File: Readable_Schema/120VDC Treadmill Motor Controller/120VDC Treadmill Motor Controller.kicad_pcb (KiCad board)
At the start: 2 copper layers, 171.2 x 90.5 mm, 60 parts, among them J1 TB005-762-03BE, J2 OSTT7020150, J3 TB0011-350-08BE, J4 TB0011-350-08BE, J5 TB0011-350-08BE, J6 TB0011-350-03BE, K1 T9GV1L14-24, Q1 IPP200N25N3GXKSA1, Q2 IPP200N25N3GXKSA1, Q3 IPP200N25N3GXKSA1, Q4 IPP200N25N3GXKSA1, U1 UCC21530DWKR, U2 UCC21530DWKR, U3 TMCS1126B42QDVGRQ1, U5 NLV14044BDR2G, U8 RAC05E-05SKT

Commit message: -Think we're finished with the schematic (finally) --Upped the LED resistors and added a few more supporting caps for the 3.3v iso supply in the feedback schema
-Started placing footprints
--Now that we're using how air instead of oven I'm not going to try and keep all SMD components on the same side anymore
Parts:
- removed R26: 10K, Resistor_SMD:R_0201_0603Metric_Pad0.64x0.40mm_HandSolder
- removed TP10, TP9: RCWCTE, Treadmill_Feet:RCWCTE
- removed U8: RAC05E-05SKT, Treadmill_Feet:RAC05E-KT_RCP
- added C14: 820uF, Treadmill_Feet:CHEMI-VSN_A45, F.Cu at (262.0, 117.4)
- added C17: 820uF, Treadmill_Feet:CHEMI-VSN_A45, F.Cu at (262.0, 154.0)
- added C18: 4.7u, Capacitor_SMD:C_0201_0603Metric_Pad0.64x0.40mm_HandSolder, F.Cu at (350.5, 57.8)
- added C19: 4.7u, Capacitor_SMD:C_0201_0603Metric_Pad0.64x0.40mm_HandSolder, F.Cu at (353.3, 43.8)
- added C20: 4.7u, Capacitor_SMD:C_0201_0603Metric_Pad0.64x0.40mm_HandSolder, F.Cu at (353.3, 45.6)
- added C21: 0.1u, Capacitor_SMD:C_0201_0603Metric_Pad0.64x0.40mm_HandSolder, F.Cu at (353.4, 113.8)
- added C22: 4.7u, Capacitor_SMD:C_0402_1005Metric_Pad0.74x0.62mm_HandSolder, F.Cu at (314.4, 54.1)
- added C23: 4.7u, Capacitor_SMD:C_0402_1005Metric_Pad0.74x0.62mm_HandSolder, F.Cu at (314.4, 56.1)
- added C24: 10u, Capacitor_SMD:C_0402_1005Metric_Pad0.74x0.62mm_HandSolder, F.Cu at (314.4, 58.1)
- added C25: 1u, Capacitor_SMD:C_0402_1005Metric_Pad0.74x0.62mm_HandSolder, F.Cu at (368.0, 61.9)
- added C26: 0.1u, Capacitor_SMD:C_0201_0603Metric_Pad0.64x0.40mm_HandSolder, F.Cu at (353.3, 47.3)
- added C27: 1u, Capacitor_SMD:C_0402_1005Metric_Pad0.74x0.62mm_HandSolder, F.Cu at (368.0, 63.9)
- added C28: C3216X7T2V104M160AA, Capacitor_SMD:C_1206_3216Metric_Pad1.33x1.80mm_HandSolder, F.Cu at (363.3, 44.6)
- added C29: 1uF, Capacitor_SMD:C_0201_0603Metric_Pad0.64x0.40mm_HandSolder, F.Cu at (353.4, 115.5)
- added C30: 22nF, Capacitor_SMD:C_0201_0603Metric_Pad0.64x0.40mm_HandSolder, F.Cu at (353.4, 117.3)
- added C31: 100pF, Capacitor_SMD:C_0201_0603Metric_Pad0.64x0.40mm_HandSolder, F.Cu at (353.4, 119.0)
- added C32: C3216X7T2V104M160AA, Capacitor_SMD:C_1206_3216Metric_Pad1.33x1.80mm_HandSolder, F.Cu at (363.3, 48.0)
- added C33: 100nF, Capacitor_SMD:C_0201_0603Metric_Pad0.64x0.40mm_HandSolder, F.Cu at (356.2, 112.0)
- added C34: 0.1u, Capacitor_SMD:C_0201_0603Metric_Pad0.64x0.40mm_HandSolder, F.Cu at (356.2, 113.8)
- added C35: 0.1u, Capacitor_SMD:C_0201_0603Metric_Pad0.64x0.40mm_HandSolder, F.Cu at (353.3, 49.1)
- added C36: 0.1u, Capacitor_SMD:C_0201_0603Metric_Pad0.64x0.40mm_HandSolder, F.Cu at (353.3, 50.8)
- added C37: 1u, Capacitor_SMD:C_0402_1005Metric_Pad0.74x0.62mm_HandSolder, F.Cu at (368.0, 65.8)
- added C38: 0.1u, Capacitor_SMD:C_0201_0603Metric_Pad0.64x0.40mm_HandSolder, F.Cu at (353.3, 52.6)
- added C39: 0.1u, Capacitor_SMD:C_0201_0603Metric_Pad0.64x0.40mm_HandSolder, F.Cu at (353.3, 54.3)
- added C40: 0.1u, Capacitor_SMD:C_0201_0603Metric_Pad0.64x0.40mm_HandSolder, F.Cu at (353.3, 56.1)
- added C41: 0.1u, Capacitor_SMD:C_0201_0603Metric_Pad0.64x0.40mm_HandSolder, F.Cu at (353.3, 57.8)
- added C42: 0.1u, Capacitor_SMD:C_0201_0603Metric_Pad0.64x0.40mm_HandSolder, F.Cu at (356.1, 43.8)
- added C43: 0.1u, Capacitor_SMD:C_0201_0603Metric_Pad0.64x0.40mm_HandSolder, F.Cu at (356.1, 45.6)
- added C44: 22n, Capacitor_SMD:C_0201_0603Metric_Pad0.64x0.40mm_HandSolder, B.Cu at (72.1, 87.0)
- added C45: 0.1u, Capacitor_SMD:C_0201_0603Metric_Pad0.64x0.40mm_HandSolder, F.Cu at (362.8, 92.5)
- added C46: 0.1u, Capacitor_SMD:C_0201_0603Metric_Pad0.64x0.40mm_HandSolder, F.Cu at (356.2, 115.5)
- added C47: 1uF, Capacitor_SMD:C_0201_0603Metric_Pad0.64x0.40mm_HandSolder, F.Cu at (356.2, 117.3)
- added C48: 100nF, Capacitor_SMD:C_0201_0603Metric_Pad0.64x0.40mm_HandSolder, F.Cu at (356.2, 119.0)
- added C49: C3216X7T2V104M160AA, Capacitor_SMD:C_1206_3216Metric_Pad1.33x1.80mm_HandSolder, F.Cu at (363.3, 51.3)
- added C50: C3216X7T2V104M160AA, Capacitor_SMD:C_1206_3216Metric_Pad1.33x1.80mm_HandSolder, F.Cu at (363.3, 54.7)
- added C51: C3216X7T2V104M160AA, Capacitor_SMD:C_1206_3216Metric_Pad1.33x1.80mm_HandSolder, F.Cu at (363.3, 58.0)
- added C52: C3216X7T2V104M160AA, Capacitor_SMD:C_1206_3216Metric_Pad1.33x1.80mm_HandSolder, F.Cu at (363.3, 61.4)
- added C53: C3216X7T2V104M160AA, Capacitor_SMD:C_1206_3216Metric_Pad1.33x1.80mm_HandSolder, F.Cu at (363.3, 64.7)
- added C54: C3216X7T2V104M160AA, Capacitor_SMD:C_1206_3216Metric_Pad1.33x1.80mm_HandSolder, F.Cu at (363.3, 68.1)
- added C6: 820uF, Treadmill_Feet:CHEMI-VSN_A45, F.Cu at (262.0, 44.4)
- added C7: 820uF, Treadmill_Feet:CHEMI-VSN_A45, F.Cu at (262.0, 80.9)
- added CR1: MMSZ5231B-7-F, Treadmill_Feet:SOD123_DIO, F.Cu at (354.8, 62.0)
- added CR2: MMSZ5231B-7-F, Treadmill_Feet:SOD123_DIO, F.Cu at (354.8, 65.0)
- added D3: MSS1P4-M3_89A, Treadmill_Feet:DIODE_MSS1P4-M3_89A, F.Cu at (369.1, 59.4)
- added D4: LED, LED_SMD:LED_1206_3216Metric_Pad1.42x1.75mm_HandSolder, F.Cu at (363.2, 73.5)
- added D5: SS12, Diode_SMD:D_SMA, B.Cu at (110.0, 65.0)
- added J7: OSTT7020150, Treadmill_Feet:CONN2_OSTT7020150_OST, F.Cu at (287.8, 55.2)
- added J9: OSTT7020150, Treadmill_Feet:CONN2_OSTT7020150_OST, F.Cu at (343.8, 90.4)
- added PS2: SRS-0509-2, Footprints_TMC:SRS-0515 DIP-16_W7.62mm, F.Cu at (349.9, 23.1)
- added PS7: IRM-15-5, Treadmill_Feet:CONV_IRM-15-5, F.Cu at (308.6, 35.5)
- added Q5: IPP60R060P7XKSA1, Package_TO_SOT_THT:TO-220-3_Vertical, F.Cu at (301.4, 60.8)
- added Q7: DN2450N8-G, Treadmill_Feet:TO-243AA_MCH, F.Cu at (358.3, 95.0)
- added Q8: VOM1271T, Treadmill_Feet:SOP-4_VIS, F.Cu at (358.9, 88.4)
- added R11: 100K, Resistor_SMD:R_0201_0603Metric_Pad0.64x0.40mm_HandSolder, B.Cu at (137.1, 122.0)
- added R12: 50, Resistor_SMD:R_0201_0603Metric_Pad0.64x0.40mm_HandSolder, B.Cu at (140.5, 118.1)
- added R17: 10K, Resistor_SMD:R_0201_0603Metric_Pad0.64x0.40mm_HandSolder, F.Cu at (356.1, 57.8)
- added R18: 10K, Resistor_SMD:R_0201_0603Metric_Pad0.64x0.40mm_HandSolder, B.Cu at (130.0, 120.9)
- added R19: 4.7, Resistor_SMD:R_1206_3216Metric_Pad1.30x1.75mm_HandSolder, F.Cu at (372.9, 29.4)
- added R20: 10, Resistor_SMD:R_1206_3216Metric_Pad1.30x1.75mm_HandSolder, F.Cu at (372.9, 32.7)
- added R21: 10, Resistor_SMD:R_1206_3216Metric_Pad1.30x1.75mm_HandSolder, F.Cu at (372.9, 36.0)
- added R22: 10, Resistor_SMD:R_1206_3216Metric_Pad1.30x1.75mm_HandSolder, F.Cu at (372.9, 39.3)
- added R28: 10K, Resistor_SMD:R_0201_0603Metric_Pad0.64x0.40mm_HandSolder, F.Cu at (320.2, 54.2)
- added R29: 10K, Resistor_SMD:R_0201_0603Metric_Pad0.64x0.40mm_HandSolder, B.Cu at (140.5, 136.1)
- added R30: 10K, Resistor_SMD:R_0201_0603Metric_Pad0.64x0.40mm_HandSolder, B.Cu at (140.5, 140.1)
- added R31: 1.2K, Resistor_SMD:R_0201_0603Metric_Pad0.64x0.40mm_HandSolder, F.Cu at (358.9, 49.1)
- added R32: 10K, Resistor_SMD:R_0201_0603Metric_Pad0.64x0.40mm_HandSolder, F.Cu at (358.9, 50.8)
- added R33: 30K, Treadmill_Feet:YAG_RSF100_YAG, F.Cu at (339.2, 75.1)
- added R34: 10K, Resistor_SMD:R_1206_3216Metric_Pad1.30x1.75mm_HandSolder, F.Cu at (355.0, 102.9)
- added R35: 500K, Resistor_SMD:R_1206_3216Metric_Pad1.30x1.75mm_HandSolder, F.Cu at (355.0, 106.2)
- added R36: 50, Resistor_SMD:R_0201_0603Metric_Pad0.64x0.40mm_HandSolder, F.Cu at (359.0, 115.5)
- added R37: 50, Resistor_SMD:R_0201_0603Metric_Pad0.64x0.40mm_HandSolder, F.Cu at (359.0, 117.3)
- added R38: 500K, Resistor_SMD:R_1206_3216Metric_Pad1.30x1.75mm_HandSolder, F.Cu at (355.0, 109.5)
- added R39: 10K, Resistor_SMD:R_0201_0603Metric_Pad0.64x0.40mm_HandSolder, B.Cu at (72.1, 81.0)
- added R40: 10K, Resistor_SMD:R_0201_0603Metric_Pad0.64x0.40mm_HandSolder, B.Cu at (72.1, 83.5)
- added R41: 3.3K, Resistor_SMD:R_0201_0603Metric_Pad0.64x0.40mm_HandSolder, B.Cu at (72.1, 132.5)
- added R42: 3.3K, Resistor_SMD:R_0201_0603Metric_Pad0.64x0.40mm_HandSolder, B.Cu at (72.1, 136.0)
- added R43: ERZ-V14D241, Treadmill_Feet:RES_ERZ-V14D241_PAN, F.Cu at (348.2, 130.8)
- added R45: 30K, Treadmill_Feet:YAG_RSF100_YAG, F.Cu at (339.2, 81.8)
- added R46: 330, Resistor_SMD:R_0201_0603Metric_Pad0.64x0.40mm_HandSolder, F.Cu at (362.8, 94.3)
- added R47: 1M, Resistor_SMD:R_0201_0603Metric_Pad0.64x0.40mm_HandSolder, F.Cu at (362.8, 96.0)
- added R48: 1K, Resistor_SMD:R_0201_0603Metric_Pad0.64x0.40mm_HandSolder, F.Cu at (362.8, 97.8)
- added R49: ERZ-V14D241, Treadmill_Feet:RES_ERZ-V14D241_PAN, F.Cu at (348.2, 137.5)
- added R50: ERZ-V14D241, Treadmill_Feet:RES_ERZ-V14D241_PAN, F.Cu at (348.2, 144.2)
- added R9: 10K, Resistor_SMD:R_0201_0603Metric_Pad0.64x0.40mm_HandSolder, F.Cu at (359.0, 112.0)
- added TP3: RCWCTE, Treadmill_Feet:RCWCTE, F.Cu at (354.9, 121.5)
- added U4: SN74HCS08DYYR, Treadmill_Feet:14-SOT-23-THIN, F.Cu at (360.8, 104.3)
- added U6: AMC1311BDWVR, Treadmill_Feet:DWV0008A, F.Cu at (344.4, 119.1)
- C1, C3, C9: value 33pF -> 33p
- C10, C16: value 0.1u -> 4.7u; footprint Capacitor_SMD:C_0402_1005Metric_Pad0.74x0.62mm_HandSolder -> Capacitor_SMD:C_0201_0603Metric_Pad0.64x0.40mm_HandSolder; moved to F.Cu
- C11: value 0.1u -> 33p; footprint Capacitor_SMD:C_0402_1005Metric_Pad0.74x0.62mm_HandSolder -> Capacitor_SMD:C_0201_0603Metric_Pad0.64x0.40mm_HandSolder
- C12: value 0.1u -> 33pF; footprint Capacitor_SMD:C_0402_1005Metric_Pad0.74x0.62mm_HandSolder -> Capacitor_SMD:C_0201_0603Metric_Pad0.64x0.40mm_HandSolder
- C13: value 33pF -> 0.1u
- C15: value 33pF -> 4.7u; moved to F.Cu
- C4: footprint Capacitor_SMD:C_0402_1005Metric_Pad0.74x0.62mm_HandSolder -> Capacitor_SMD:C_0201_0603Metric_Pad0.64x0.40mm_HandSolder; moved to F.Cu
- C5: footprint Capacitor_SMD:C_0402_1005Metric_Pad0.74x0.62mm_HandSolder -> Capacitor_SMD:C_0201_0603Metric_Pad0.64x0.40mm_HandSolder
- D2: value 1N5817 -> MSS1P4-M3_89A; footprint Diode_THT:D_DO-41_SOD81_P10.16mm_Horizontal -> Treadmill_Feet:DIODE_MSS1P4-M3_89A
- PS4: value SRS-0515-2 -> DHP1-5-S3-M; footprint Footprints_TMC:SRS-0515 DIP-16_W7.62mm -> Treadmill_Feet:CONV_DHP1-5-S3-M
- Q1, Q2, Q3, Q4: value IPP200N25N3GXKSA1 -> IPP60R060P7XKSA1
- R10: value 10K -> 4.7; footprint Resistor_SMD:R_0201_0603Metric_Pad0.64x0.40mm_HandSolder -> Resistor_SMD:R_1206_3216Metric_Pad1.30x1.75mm_HandSolder; moved to F.Cu
- R15: value 10K -> 10; footprint Resistor_SMD:R_0201_0603Metric_Pad0.64x0.40mm_HandSolder -> Resistor_SMD:R_1206_3216Metric_Pad1.30x1.75mm_HandSolder; moved to F.Cu
- R23, R27: moved to F.Cu
- R24: footprint Resistor_SMD:R_0201_0603Metric_Pad0.64x0.40mm_HandSolder -> Resistor_SMD:R_1206_3216Metric_Pad1.30x1.75mm_HandSolder; moved to F.Cu
- R25: value 10 -> 20K; moved to F.Cu
- R4: value 50 -> 10K
- R7: value 10 -> 1.2K; moved to F.Cu
- R8: value 10 -> 10K
- U5: value NLV14044BDR2G -> TPSI3050QDWZRQ1; footprint Treadmill_Feet:SOIC-16_ONS -> Treadmill_Feet:DWZ0008A-IPC_A; moved to F.Cu
- moved PS3 298.8 mm to (360.7, 23.1), turned to 0 degrees
- moved PS1 284.3 mm to (339.1, 23.1), turned to 0 degrees
- moved PS4 262.0 mm to (345.2, 108.4), turned to 0 degrees
- moved D2 260.9 mm to (369.1, 56.5), turned to 0 degrees
- moved C4 240.2 mm to (353.4, 112.0), turned to 0 degrees
- moved R15 230.0 mm to (372.9, 26.1)
- moved R23 222.9 mm to (359.0, 113.8), turned to 0 degrees
- moved C16 222.1 mm to (350.5, 56.1), turned to 0 degrees
- moved C15 217.3 mm to (350.5, 54.3), turned to 0 degrees
- moved R10 210.7 mm to (372.9, 22.7)
- moved U5 194.8 mm to (305.9, 53.3), turned to 0 degrees
- moved Q4 194.1 mm to (340.8, 64.7), turned to 0 degrees
- moved R25 188.9 mm to (320.2, 50.7)
- moved R7 187.8 mm to (356.1, 49.1)
- moved Q3 185.3 mm to (340.8, 58.8), turned to 0 degrees
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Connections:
- A1 pad 1: unconnected-(A1-GPIO0-Pad1) -> /Pi Pico/GP0
- A1 pad 11: unconnected-(A1-GPIO8-Pad11) -> Net-(A1-GPIO8)
- A1 pad 12: unconnected-(A1-GPIO9-Pad12)_1 -> Net-(A1-GPIO9)
- A1 pad 2: unconnected-(A1-GPIO1-Pad2) -> /Feedback/mcu_en
- A1 pad 26: unconnected-(A1-GPIO20-Pad26) -> /Pi Pico/pre_charge_mcu
- A1 pad 33: /Pi Pico/ADC_GND -> /Feedback/adc_gnd
- A1 pad 34: /Pi Pico/pot_adc -> /Feedback/cap_vsense
- C10 pad 1: /H_Bridge/hs_ps_2_+ -> /H_Bridge/ls_ps_+
- C10 pad 2: /H_Bridge/hs_ps_2_- -> /Feedback/in+
- C11 pad 1: /H_Bridge/hs_ps_1_+ -> Net-(U1-INB)
- C11 pad 2: /H_Bridge/hs_ps_1_- -> LV_GND
- C12 pad 1: /H_Bridge/ls_ps_+ -> Net-(U1-DT)
- C12 pad 2: HV_GND -> LV_GND
- C13 pad 1: Net-(U1-INB) -> 5v 15w
- C15 pad 1: Net-(U1-DT) -> /H_Bridge/hs_ps_2_+
- C15 pad 2: LV_GND -> Net-(J2-Pin_2)
- C16 pad 1: 5v 5w -> Net-(J2-Pin_2)
- C16 pad 2: LV_GND -> /H_Bridge/hs_ps_2_-
- C5 pad 1: 5v 5w -> 5v 15w
- D1 pad 1: 170V Rect -> Net-(D1-+)
- D2 pad 1: Net-(A1-VSYS) -> Net-(D2-Pad1)
- D2 pad 2: 5v 5w -> Net-(Q2-G)
- J1 pad 3: unconnected-(J1-Pin_3-Pad3) -> Net-(J1-Pin_3)
- J2 pad 1: /H_Bridge/hs_ps_1_- -> Net-(J2-Pin_1)
- J2 pad 2: /H_Bridge/hs_ps_2_- -> Net-(J2-Pin_2)
- J3 pad 1: 5v 5w -> 5v 15w
- J3 pad 5: 5v 5w -> 5v 15w
- J4 pad 1: /Pi Pico/pot_adc -> Net-(A1-GPIO8)
- J4 pad 2: /Pi Pico/ADC_GND -> Net-(A1-GPIO9)
- J5 pad 7: /Pi Pico/ADC_GND -> /Feedback/adc_gnd
- J5 pad 8: 3v3 MCU -> /Pi Pico/GP0
- J6 pad 3: 5v 5w -> 5v 15w
- JP2 pad 2: /Pi Pico/ADC_GND -> /Feedback/adc_gnd
- PS1 pad 1: 5v 5w -> 5v 15w
- PS1 pad 11: HV_GND -> /H_Bridge/hs_ps_1_-
- PS1 pad 7: /H_Bridge/ls_ps_+ -> /H_Bridge/hs_ps_1_+
- PS3 pad 1: 5v 5w -> 5v 15w
- PS3 pad 11: /H_Bridge/hs_ps_1_- -> /H_Bridge/hs_ps_2_-
- PS3 pad 7: /H_Bridge/hs_ps_1_+ -> /H_Bridge/hs_ps_2_+
- PS4 pad 1: 5v 5w -> LV_GND
- Q1 pad 1: 170V Rect -> Net-(Q1-G)
- Q1 pad 2: Net-(Q1-G) -> Net-(J2-Pin_1)
- Q1 pad 3: /H_Bridge/hs_ps_2_- -> /Feedback/in+
- Q2 pad 1: 170V Rect -> Net-(Q2-G)
- Q2 pad 2: Net-(Q2-G) -> 170V Rect
- Q2 pad 3: /H_Bridge/hs_ps_1_- -> Net-(J2-Pin_1)
- Q3 pad 1: /H_Bridge/hs_ps_1_- -> Net-(Q3-G)
- Q3 pad 2: Net-(Q3-G) -> 170V Rect
- Q3 pad 3: /Feedback/in+ -> Net-(J2-Pin_2)
- Q4 pad 1: /H_Bridge/hs_ps_2_- -> Net-(Q4-G)
- Q4 pad 2: Net-(Q4-G) -> Net-(J2-Pin_2)
- R10 pad 1: /H_Bridge/hs_ps_1_- -> Net-(U2-OUTA)
- R10 pad 2: Net-(Q2-G) -> Net-(D2-Pad1)
- R13 pad 1: 5v 5w -> 5v 15w
- R15 pad 1: /Feedback/in+ -> Net-(Q2-G)
- R15 pad 2: Net-(Q3-G) -> Net-(U2-OUTA)
- R23 pad 1: Net-(U1-DT) -> /Feedback/mcu_en
- R24 pad 1: Net-(U1-OUTA) -> Net-(U5-VDRV)
- R24 pad 2: Net-(Q1-G) -> Net-(Q5-G)
- R25 pad 1: Net-(U1-OUTB) -> Net-(U5-PXFR)
- R25 pad 2: Net-(Q4-G) -> LV_GND
- R27 pad 1: /Feedback/in+ -> Net-(Q5-G)
- R27 pad 2: Net-(Q4-G) -> 170V Rect
- R4 pad 2: Net-(U1-INA) -> LV_GND
- R7 pad 1: Net-(U2-OUTA) -> /H_Bridge/hs_ps_1_+
- R7 pad 2: Net-(Q2-G) -> Net-(J2-Pin_1)
- R8 pad 1: Net-(U2-OUTB) -> /H_Bridge/dir_a
- R8 pad 2: Net-(Q3-G) -> LV_GND
- TP1 pad 1: /H_Bridge/hs_ps_1_- -> Net-(J2-Pin_1)
- TP2 pad 1: /H_Bridge/hs_ps_2_- -> Net-(J2-Pin_2)
- U1 pad 3: 5v 5w -> 5v 15w
- U2 pad 3: 5v 5w -> 5v 15w
- U3 pad 4: 5v 5w -> 5v 15w
- U3 pad 7: LV_GND -> unconnected-(U3-VREF-Pad7)
- U5 pad 1: unconnected-(U5-Q3-Pad1) -> /Pi Pico/pre_charge_mcu
- U5 pad 2: unconnected-(U5-NC-Pad2) -> Net-(U5-PXFR)
- U5 pad 3: /Feedback/Set -> 5v 15w
- U5 pad 4: /Feedback/Reset -> LV_GND
- U5 pad 5: /Feedback/OC_out -> 170V Rect
- U5 pad 6: unconnected-(U5-*R1-Pad6) -> Net-(U5-VDDM)
- U5 pad 7: unconnected-(U5-*S1-Pad7) -> Net-(U5-VDDH)
- U5 pad 8: LV_GND -> Net-(U5-VDRV)
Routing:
- net LV_GND: track 0.00 -> 21.9 mm
- net /H_Bridge/EN_drive: track 0.00 -> 20.7 mm
- net Net-(U2-INA): track 0.00 -> 12.4 mm
- net Net-(U2-DT): track 0.00 -> 4.40 mm
- net Net-(A1-VSYS): track 4.50 -> 0.28 mm
- net Net-(U2-INB): track 0.00 -> 2.92 mm
- net 5v 15w: track 0.00 -> 2.41 mm
- net /H_Bridge/pwm_a: track 0.00 -> 2.00 mm
- net /H_Bridge/dir_b: track 0.00 -> 2.00 mm
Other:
- board size 171.2 x 90.5 mm -> 171.2 x 104 mm

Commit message: -placed more components surrounding the H bridge, thinking may have placed things a little too close to each. I think it may be time to figure out vias so that I can use both sides of the board lol. Looking like track widths are going to be quite large at 0.762 mm
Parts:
- C10, C15, C16, C18, C19, C20, C26, C27, C35, C36, C37, C38, C39, C41, C42, C43, CR1, CR2, D2, D3, R10, R15, R17, R19, R20, R21, R22, R31, R32, R7: moved to B.Cu
- moved R19 246.1 mm to (160.0, 152.8), turned to 180 degrees
- moved R21 239.3 mm to (165.9, 156.0), turned to 180 degrees
- moved R10 235.9 mm to (176.1, 152.9), turned to 180 degrees
- moved R15 230.8 mm to (182.2, 156.2), turned to 180 degrees
- moved D3 230.4 mm to (159.8, 156.0)
- moved C42 219.1 mm to (164.1, 149.2), turned to 180 degrees
- moved D2 217.1 mm to (176.2, 156.2)
- moved R31 216.1 mm to (169.3, 152.8)
- moved R20 216.0 mm to (195.5, 155.9), turned to 90 degrees
- moved C27 214.7 mm to (170.9, 149.2), turned to 180 degrees
- moved PS3 212.6 mm to (175.4, 127.4)
- moved CR2 212.3 mm to (159.9, 149.2), turned to 180 degrees
- moved C16 209.8 mm to (164.3, 152.8), turned to 180 degrees
- moved C15 208.4 mm to (166.8, 152.8), turned to 180 degrees
- moved C41 207.2 mm to (167.4, 149.2)
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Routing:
- net LV_GND: track 21.9 -> 67.5 mm
- net /H_Bridge/EN_drive: track 20.7 -> 39.6 mm
- net Net-(U2-INB): track 2.92 -> 21.2 mm
- net Net-(U1-INA): track 0.00 -> 11.6 mm
- net Net-(U1-INB): track 0.00 -> 5.80 mm
- net Net-(U1-DT): track 0.00 -> 4.46 mm
- net 5v 15w: track 2.41 -> 5.67 mm
- net /H_Bridge/pwm_b: track 0.00 -> 2.28 mm
- net /H_Bridge/dir_a: track 0.00 -> 2.25 mm
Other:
- outline, holes or cut-outs redrawn

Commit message: -Getting fairly stuck on the best way to layout some of these high voltage components, especially the high current line that requires a pour rather than a trace
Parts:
- added NT1: NetTie_2, NetTie:NetTie-2_THT_Pad0.3mm, F.Cu at (171.5, 167.6)
- added NT2: NetTie_2, NetTie:NetTie-2_THT_Pad0.3mm, F.Cu at (171.5, 169.2)
- added NT3: NetTie_2, NetTie:NetTie-2_THT_Pad0.3mm, F.Cu at (171.5, 170.8)
- added NT4: NetTie_2, NetTie:NetTie-2_THT_Pad0.3mm, F.Cu at (171.5, 172.3)
- moved J2 120.9 mm to (228.3, 149.6)
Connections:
- C10 pad 2: /Feedback/in+ -> Net-(U2-VSSB)
- C15 pad 2: Net-(J2-Pin_2) -> Net-(C15-Pad2)
- C16 pad 1: Net-(J2-Pin_2) -> Net-(C15-Pad2)
- C18 pad 1: Net-(J2-Pin_1) -> Net-(C18-Pad1)
- C19 pad 2: Net-(J2-Pin_1) -> Net-(C18-Pad1)
- C20 pad 2: /Feedback/in+ -> Net-(U1-VSSB)
- C26 pad 1: Net-(J2-Pin_1) -> Net-(C18-Pad1)
- C35 pad 2: /Feedback/in+ -> Net-(U2-VSSB)
- C36 pad 2: Net-(J2-Pin_1) -> Net-(C18-Pad1)
- C41 pad 2: Net-(J2-Pin_2) -> Net-(C15-Pad2)
- C42 pad 1: Net-(J2-Pin_2) -> Net-(C15-Pad2)
- C43 pad 2: /Feedback/in+ -> Net-(U1-VSSB)
- CR1 pad 1: Net-(J2-Pin_1) -> Net-(C18-Pad1)
- CR2 pad 1: Net-(J2-Pin_2) -> Net-(C15-Pad2)
- R17 pad 1: /Feedback/in+ -> Net-(U2-VSSB)
- R31 pad 2: Net-(J2-Pin_2) -> Net-(C15-Pad2)
- R32 pad 1: /Feedback/in+ -> Net-(U1-VSSB)
- R7 pad 2: Net-(J2-Pin_1) -> Net-(C18-Pad1)
- U1 pad 9: /Feedback/in+ -> Net-(U1-VSSB)
- U2 pad 9: /Feedback/in+ -> Net-(U2-VSSB)
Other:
- outline, holes or cut-outs redrawn

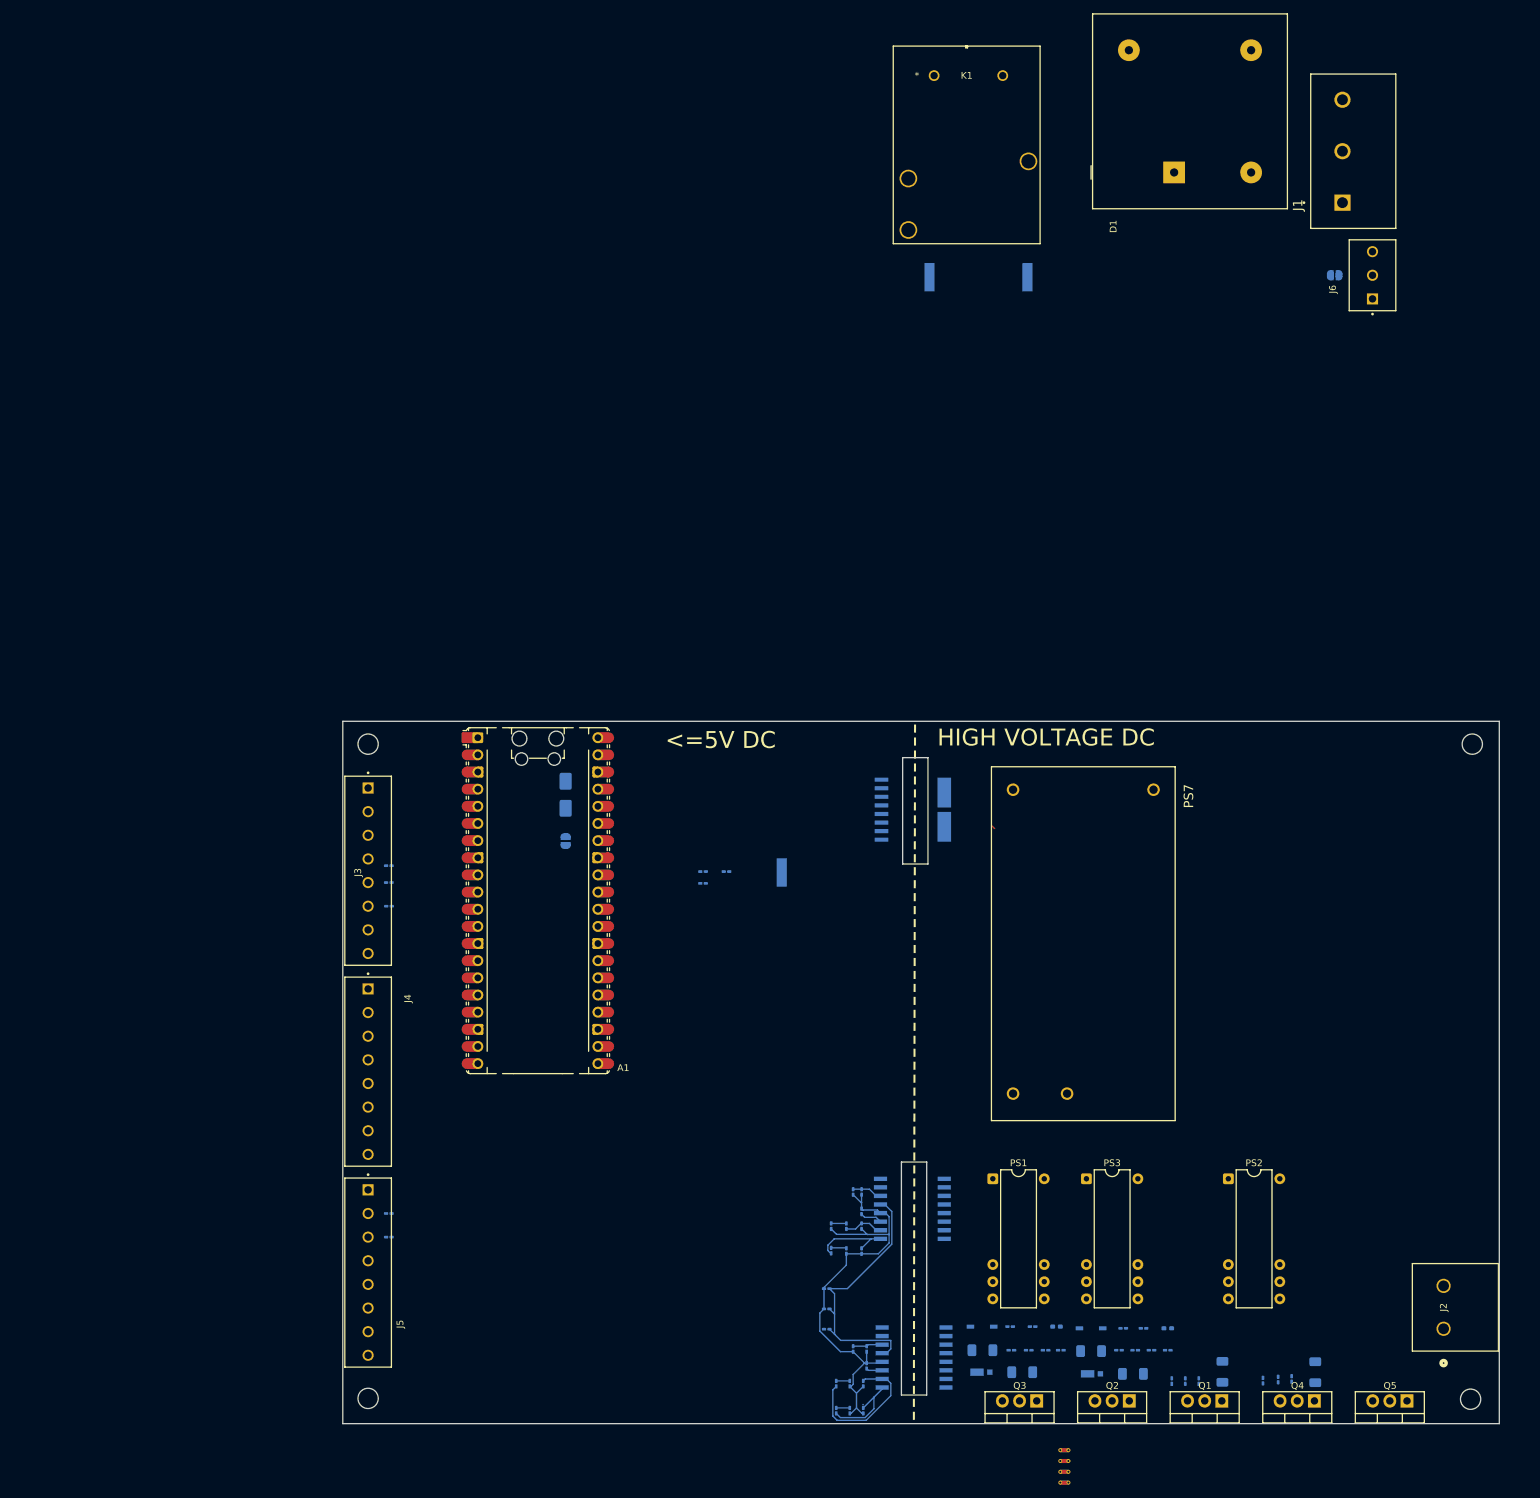
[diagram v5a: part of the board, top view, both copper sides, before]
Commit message: -Rotated a few components --Playing with different layout ideas, no major changes
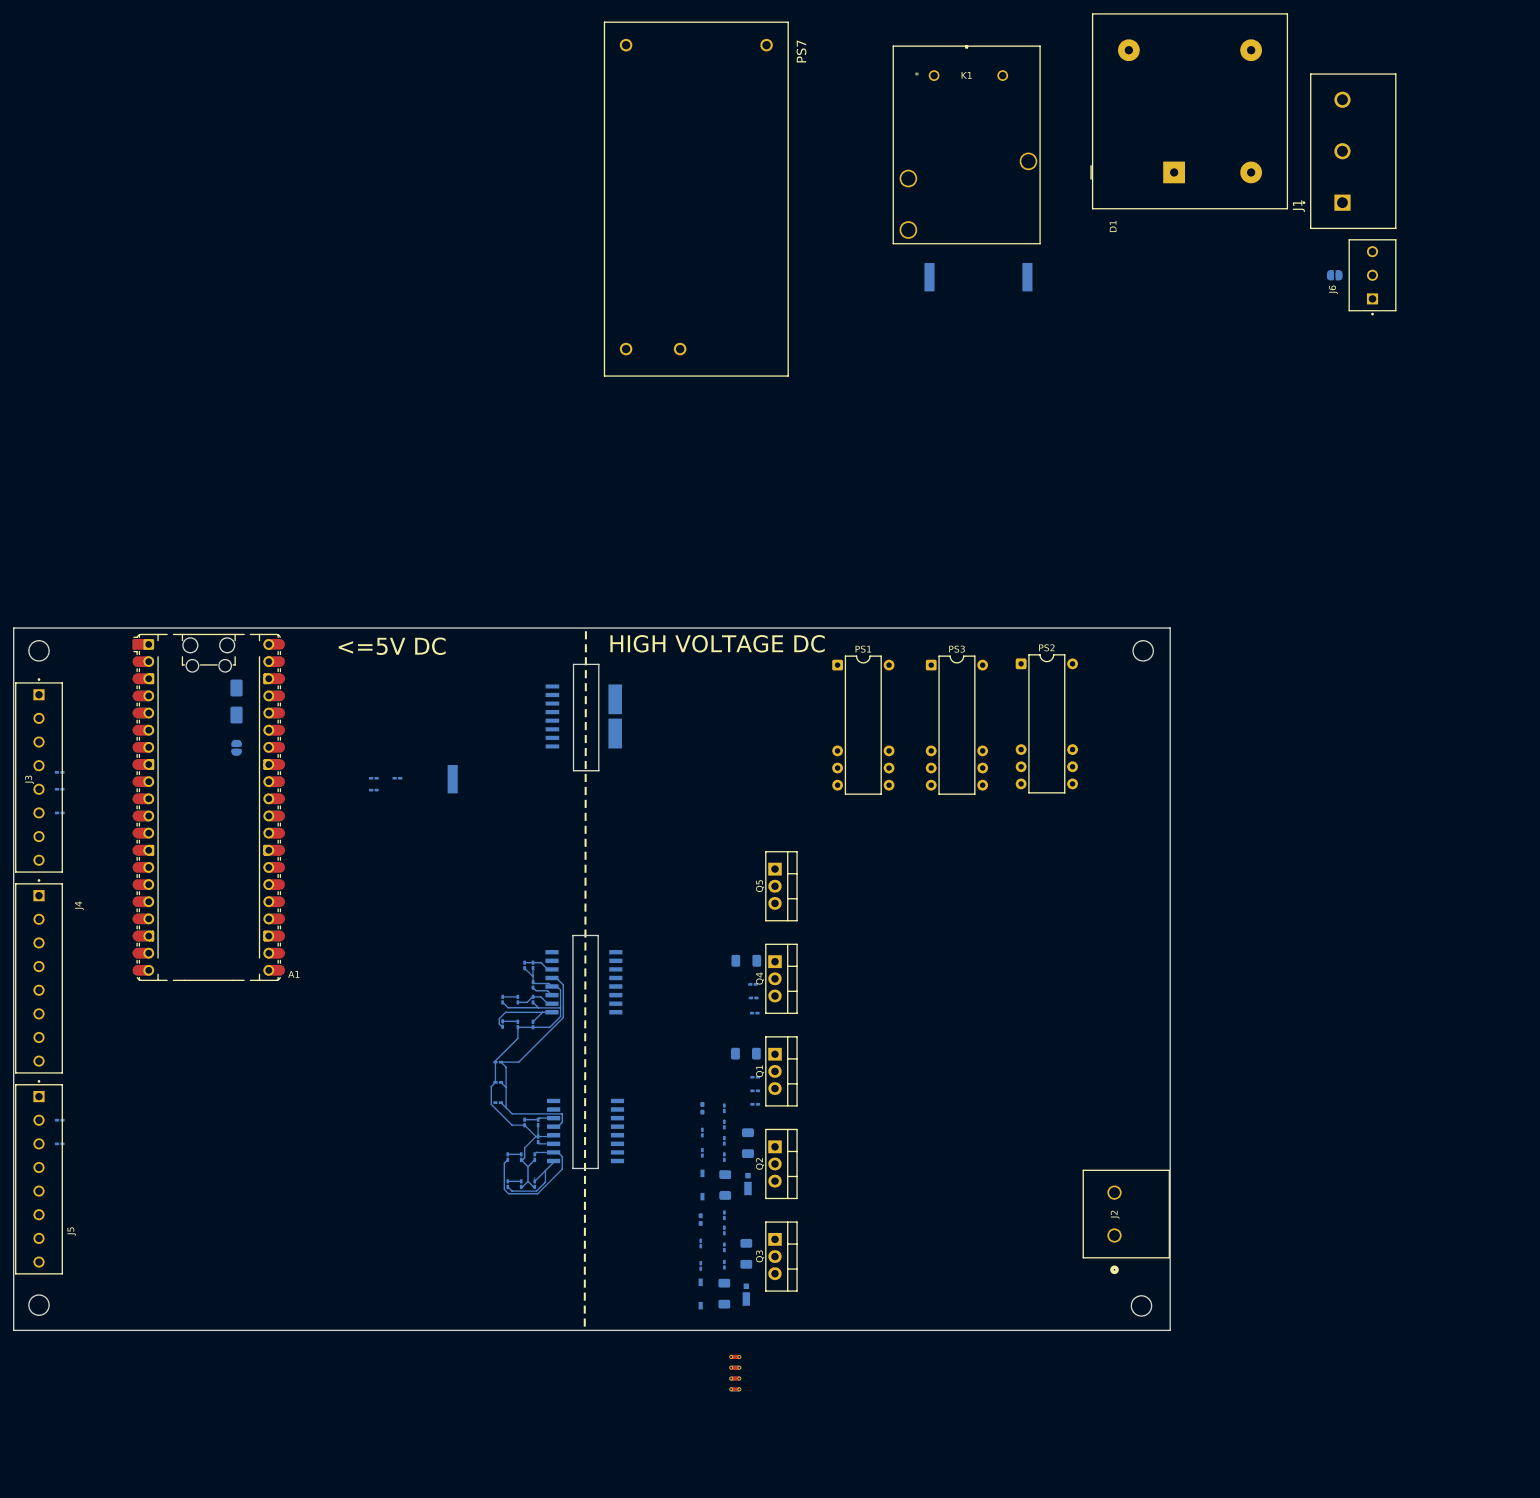
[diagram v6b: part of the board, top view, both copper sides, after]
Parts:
- moved PS7 124.3 mm to (117.6, -17.7)
- moved Q5 122.3 mm to (129.2, 81.5), turned to -90 degrees
- moved R22 104.0 mm to (125.0, 95.1), turned to 0 degrees
- moved Q4 103.0 mm to (129.2, 95.2), turned to -90 degrees
- moved C43 98.9 mm to (126.0, 98.6), turned to 180 degrees
- moved C20 96.0 mm to (126.1, 100.6), turned to 0 degrees
- moved R32 92.9 mm to (126.2, 102.8), turned to 180 degrees
- moved R20 84.8 mm to (125.0, 108.8), turned to 180 degrees
- moved Q1 83.7 mm to (129.2, 108.9), turned to -90 degrees
- moved PS2 82.2 mm to (165.7, 51.1)
- moved C35 79.6 mm to (126.3, 112.3), turned to 0 degrees
- moved PS1 79.5 mm to (138.5, 51.3)
- moved PS3 79.5 mm to (152.4, 51.3)
- moved C10 76.8 mm to (126.3, 114.3), turned to 0 degrees
- moved C37 76.2 mm to (118.5, 116.9), turned to -90 degrees
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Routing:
- net 5v 5w: track 0.59 -> 0.00 mm
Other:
- outline, holes or cut-outs redrawn

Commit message: -Finally figured out how to use a board fill. Despite having changed number of board layers at home and adding the netclasses, those board settings aren't showing up here --If board settings arent globally updated after this push then we need to do some work to understand the problem.
-Repositioning components to try and get them to share similar pours

-Still need to figure out how to set things up to be able to add solder to the High current lines
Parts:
- removed C36, C41: 0.1u, Capacitor_SMD:C_0201_0603Metric_Pad0.64x0.40mm_HandSolder
- moved C50 263.8 mm to (103.5, 100.1), turned to -90 degrees
- moved C51 262.3 mm to (103.5, 93.7), turned to 90 degrees
- moved C49 261.1 mm to (106.8, 100.1), turned to -90 degrees
- moved C52 258.5 mm to (106.8, 93.7), turned to 90 degrees
- moved C32 258.5 mm to (110.2, 100.1), turned to -90 degrees
- moved C28 255.9 mm to (113.5, 100.1), turned to -90 degrees
- moved C53 254.8 mm to (110.2, 93.7), turned to 90 degrees
- moved C54 251.1 mm to (113.5, 93.7), turned to 90 degrees
- moved NT1 185.3 mm to (302.1, 107.0)
- moved NT2 185.3 mm to (302.1, 108.7)
- moved NT3 185.3 mm to (302.1, 110.2)
- moved NT4 185.3 mm to (302.1, 111.8)
- moved C17 168.3 mm to (113.2, 75.2)
- moved PS3 125.4 mm to (86.6, 158.1)
- moved D1 116.2 mm to (230.1, 86.8)
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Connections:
- NT1 pad 2: Net-(J2-Pin_1) -> Net-(J2-Pin_2)
- NT2 pad 1: Net-(J2-Pin_2) -> Net-(J2-Pin_1)
- Q1 pad 2: Net-(J2-Pin_1) -> Net-(J2-Pin_2)
- Q2 pad 3: Net-(J2-Pin_1) -> Net-(J2-Pin_2)
- Q3 pad 3: Net-(J2-Pin_2) -> Net-(J2-Pin_1)
- Q4 pad 2: Net-(J2-Pin_2) -> Net-(J2-Pin_1)
- TP1 pad 1: Net-(J2-Pin_1) -> Net-(J2-Pin_2)
- TP2 pad 1: Net-(J2-Pin_2) -> Net-(J2-Pin_1)
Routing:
- net unconnected-(U2-VCCI_2-Pad8): track 0.00 -> 6.71 mm
- net LV_GND: track 67.5 -> 60.8 mm
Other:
- board size 171.2 x 104 mm -> 250.8 x 133.2 mm
- copper layers 2 -> 4
